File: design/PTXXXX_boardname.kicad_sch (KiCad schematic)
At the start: 14 parts

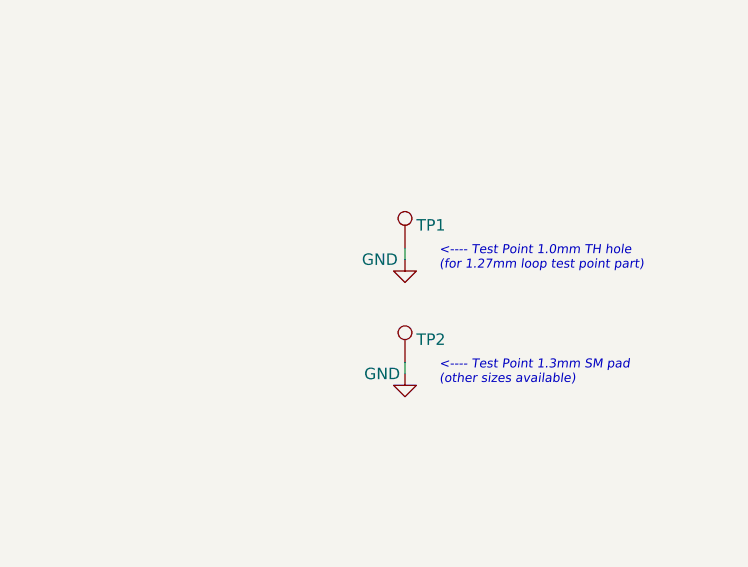
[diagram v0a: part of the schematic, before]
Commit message: migrate DNF 'FitPart'; use KiCAD v9 DNP field... ...or exclude from BOM (depending on part) updated all parts from library also removed FitPart from schematic field names update library ref for latest incl DNF/DNP changes
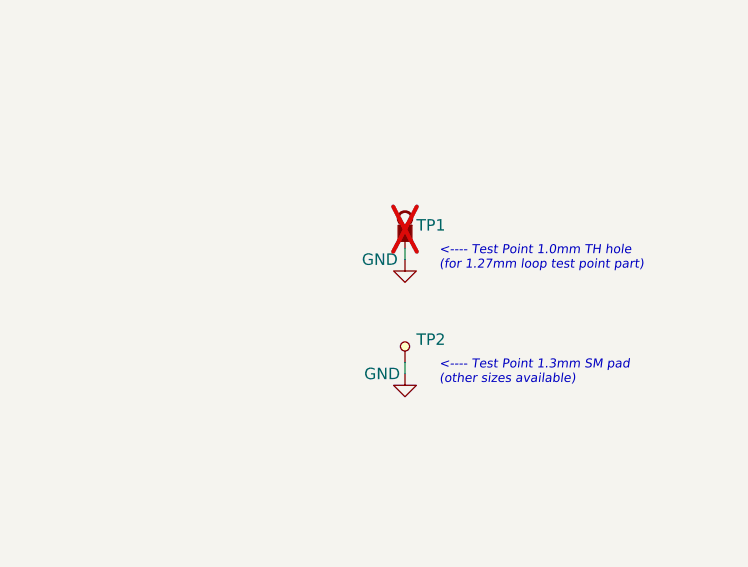
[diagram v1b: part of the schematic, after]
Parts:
- FID1, FID2, FID3, FID4, FID5, FID6, H1, H2, H3, H4, LOGO1, LOGO2, TP2: FitPart DNF -> (none); now left out of the parts list
- TP1: FitPart (none) -> (none); now not fitted
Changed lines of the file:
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@@
 		(unit 1)
 		(exclude_from_sim no)
-		(in_bom yes)
+		(in_bom no)
 		(on_board yes)
 		(dnp no)
@@
 		)
 		(property "MPN1" "N/A"
-			(at 36.83 176.53 0)
-			(effects
-				(font
-					(size 1.27 1.27)
-				)
-				(hide yes)
-			)
-		)
-		(property "FitPart" "DNF"
 			(at 36.83 176.53 0)
 			(effects
@@
 		(unit 1)
 		(exclude_from_sim no)
-		(in_bom yes)
+		(in_bom no)
 		(on_board yes)
 		(dnp no)
@@
 		)
 		(property "MPN1" "N/A"
-			(at 49.53 176.53 0)
-			(effects
-				(font
-					(size 1.27 1.27)
-				)
-				(hide yes)
-			)
-		)
-		(property "FitPart" "DNF"
 			(at 49.53 176.53 0)
 			(effects
@@
 		(unit 1)
 		(exclude_from_sim no)
-		(in_bom yes)
+		(in_bom no)
 		(on_board yes)
 		(dnp no)
@@
 		)
 		(property "MPN1" "N/A"
-			(at 62.23 176.53 0)
-			(effects
-				(font
-					(size 1.27 1.27)
-				)
-				(hide yes)
-			)
-		)
-		(property "FitPart" "DNF"
 			(at 62.23 176.53 0)
 			(effects
@@
 		(unit 1)
 		(exclude_from_sim no)
-		(in_bom yes)
+		(in_bom no)
 		(on_board yes)
 		(dnp no)
@@
 		)
 		(property "MPN1" "N/A"
-			(at 74.93 176.53 0)
-			(effects
-				(font
-					(size 1.27 1.27)
-				)
-				(hide yes)
-			)
-		)
-		(property "FitPart" "DNF"
 			(at 74.93 176.53 0)
 			(effects
@@
 		(unit 1)
 		(exclude_from_sim no)
-		(in_bom yes)
+		(in_bom no)
 		(on_board yes)
 		(dnp no)
@@
 		)
 		(property "SKU2" " "
-			(at 100.33 173.99 0)
-			(effects
-				(font
-					(size 1.27 1.27)
-				)
-				(hide yes)
-			)
-		)
-		(property "FitPart" "DNF"
 			(at 100.33 173.99 0)
 			(effects
@@
 		(unit 1)
 		(exclude_from_sim no)
-		(in_bom yes)
+		(in_bom no)
 		(on_board yes)
 		(dnp no)
@@
 		(property "SKU2" " "
 			(at 142.24 173.99 0)
-			(effects
-				(font
-					(size 1.27 1.27)
-				)
-				(hide yes)
-			)
-		)
-		(property "FitPart" "DNF"
-			(at 142.24 177.8 0)
 			(effects
 				(font
@@
 		(unit 1)
 		(exclude_from_sim no)
-		(in_bom yes)
+		(in_bom no)
 		(on_board yes)
 		(dnp no)
@@
 		(property "SKU2" " "
 			(at 132.08 181.61 0)
-			(effects
-				(font
-					(size 1.27 1.27)
-				)
-				(hide yes)
-			)
-		)
-		(property "FitPart" "DNF"
-			(at 132.08 185.42 0)
 			(effects
 				(font
@@
 		(unit 1)
 		(exclude_from_sim no)
-		(in_bom yes)
+		(in_bom no)
 		(on_board yes)
 		(dnp no)
@@
 		(property "SKU2" " "
 			(at 132.08 173.99 0)
-			(effects
-				(font
-					(size 1.27 1.27)
-				)
-				(hide yes)
-			)
-		)
-		(property "FitPart" "DNF"
-			(at 132.08 177.8 0)
 			(effects
 				(font
@@
 		(unit 1)
 		(exclude_from_sim no)
-		(in_bom yes)
+		(in_bom no)
 		(on_board yes)
 		(dnp no)
@@
 		)
 		(property "SKU2" " "
-			(at 100.33 180.34 0)
-			(effects
-				(font
-					(size 1.27 1.27)
-				)
-				(hide yes)
-			)
-		)
-		(property "FitPart" "DNF"
 			(at 100.33 180.34 0)
 			(effects
@@
 		(in_bom yes)
 		(on_board yes)
-		(dnp no)
+		(dnp yes)
 		(property "Reference" "TP1"
 			(at 219.71 115.57 0)
@@
 		)
 		(property "SKU2" "534-5001"
-			(at 217.17 124.46 0)
-			(effects
-				(font
-					(size 1.27 1.27)
-				)
-				(hide yes)
-			)
-		)
-		(property "FitPart" " "
 			(at 217.17 124.46 0)
 			(effects
@@
 		(unit 1)
 		(exclude_from_sim no)
-		(in_bom yes)
+		(in_bom no)
 		(on_board yes)
 		(dnp no)
@@
 		(property "SKU2" " "
 			(at 142.24 181.61 0)
-			(effects
-				(font
-					(size 1.27 1.27)
-				)
-				(hide yes)
-			)
-		)
-		(property "FitPart" "DNF"
-			(at 142.24 185.42 0)
 			(effects
 				(font
@@
 		(unit 1)
 		(exclude_from_sim no)
-		(in_bom yes)
+		(in_bom no)
 		(on_board yes)
 		(dnp no)
@@
 		(property "SKU2" " "
 			(at 132.08 177.8 0)
-			(effects
-				(font
-					(size 1.27 1.27)
-				)
-				(hide yes)
-			)
-		)
-		(property "FitPart" "DNF"
-			(at 132.08 181.61 0)
 			(effects
 				(font
@@
 		(unit 1)
 		(exclude_from_sim no)
-		(in_bom yes)
+		(in_bom no)
 		(on_board yes)
 		(dnp no)
@@
 		)
 		(property "SKU2" " "
-			(at 219.71 137.16 0)
-			(effects
-				(font
-					(size 1.27 1.27)
-				)
-				(hide yes)
-			)
-		)
-		(property "FitPart" "DNF"
 			(at 219.71 137.16 0)
 			(effects
@@
 		(unit 1)
 		(exclude_from_sim no)
-		(in_bom yes)
+		(in_bom no)
 		(on_board yes)
 		(dnp no)
@@
 			(effects
 				(font
-					(size 1.27 1.27)
-				)
-				(hide yes)
-			)
-		)
-		(property "FitPart" "DNF"
-			(at 142.24 181.61 0)
-			(effects
-				(font

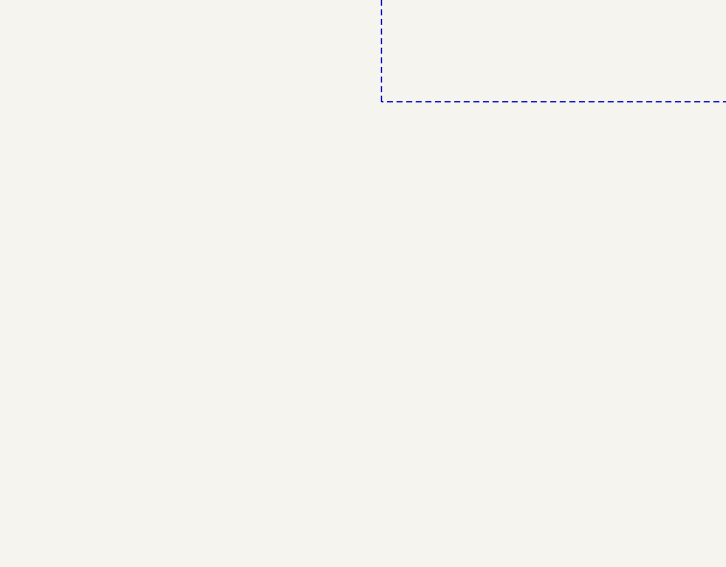
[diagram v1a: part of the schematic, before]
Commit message: added schematic table example (I2C Bus Table) replaced layout fabrication text with table
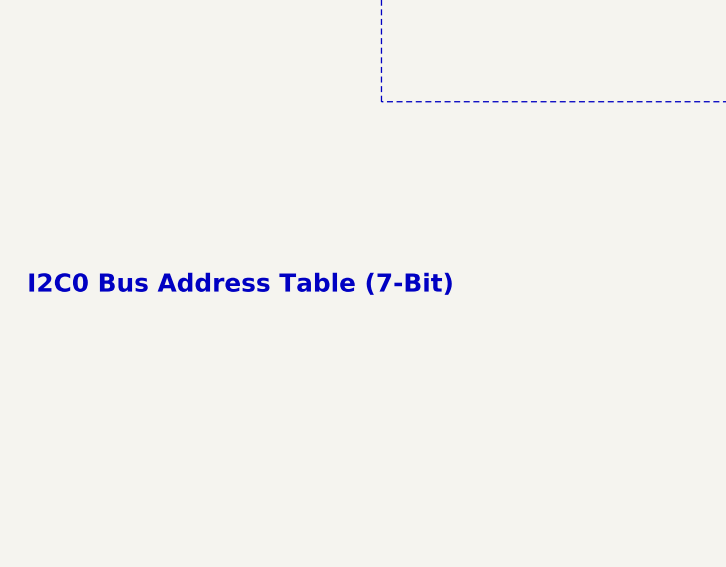
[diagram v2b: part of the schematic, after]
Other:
- note added: "I2C0 Bus Address Table (7-Bit)"
